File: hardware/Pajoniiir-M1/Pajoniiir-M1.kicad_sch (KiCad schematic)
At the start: 0 parts

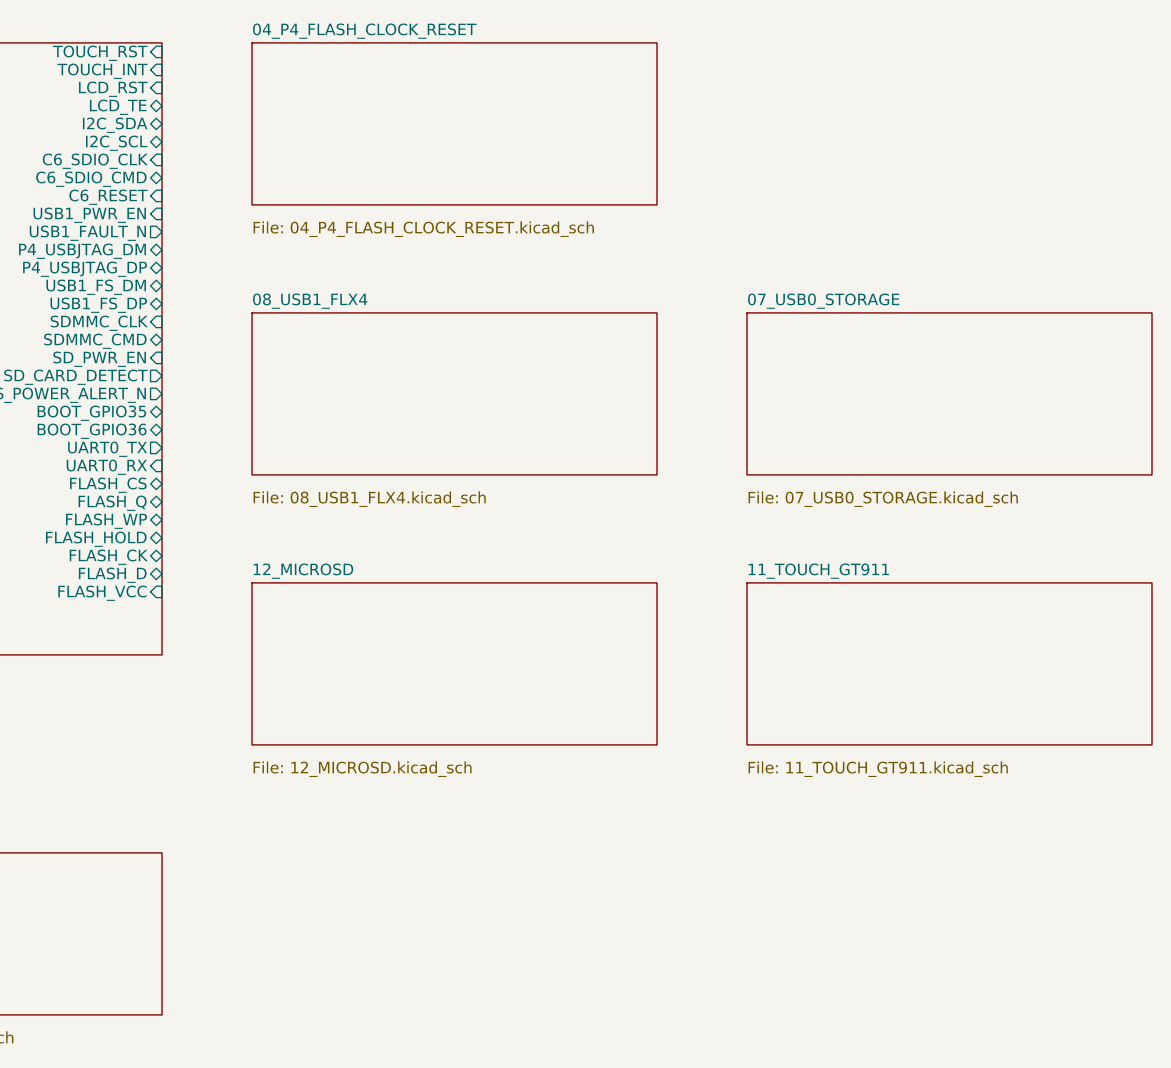
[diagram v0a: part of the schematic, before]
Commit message: hardware: capture P4 flash clock reset boot schematic
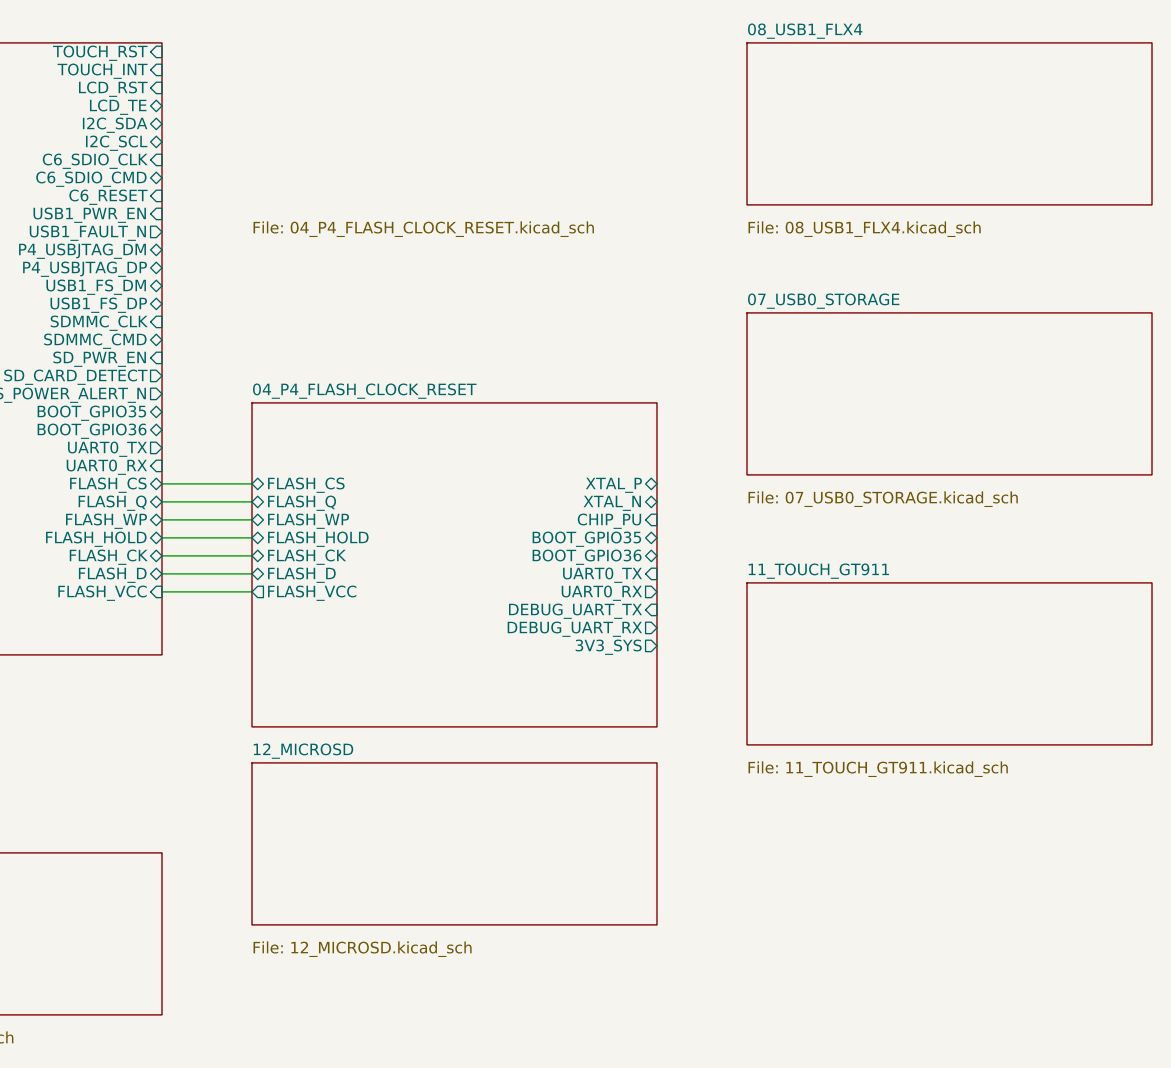
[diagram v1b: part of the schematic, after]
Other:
- sheet 04_P4_FLASH_CLOCK_RESET ports: added 3V3_SYS, BOOT_GPIO35, BOOT_GPIO36, CHIP_PU, DEBUG_UART_RX, DEBUG_UART_TX, FLASH_CK, FLASH_CS, FLASH_D, FLASH_HOLD, FLASH_Q, FLASH_VCC, FLASH_WP, UART0_RX, UART0_TX, XTAL_N, XTAL_P; removed none
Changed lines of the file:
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@@
   )
   (sheet
-    (at 185 20)
-    (size 45 18)
+    (at 185 60)
+    (size 45 36)
     (fields_autoplaced yes)
     (stroke (width 0.1524) (type solid))
     (fill (color 0 0 0 0.0000))
     (property "Sheetname" "04_P4_FLASH_CLOCK_RESET"
-      (at 185 19.2888 0)
+      (at 185 59.2888 0)
       (effects (font (size 1.27 1.27)) (justify left bottom))
     )
@@
       (effects (font (size 1.27 1.27)) (justify left top))
     )
+    (pin "FLASH_CS" bidirectional (at 185 69 180) (effects (font (size 1.27 1.27)) (justify left)))
+    (pin "FLASH_Q" bidirectional (at 185 71 180) (effects (font (size 1.27 1.27)) (justify left)))
+    (pin "FLASH_WP" bidirectional (at 185 73 180) (effects (font (size 1.27 1.27)) (justify left)))
+    (pin "FLASH_HOLD" bidirectional (at 185 75 180) (effects (font (size 1.27 1.27)) (justify left)))
+    (pin "FLASH_CK" bidirectional (at 185 77 180) (effects (font (size 1.27 1.27)) (justify left)))
+    (pin "FLASH_D" bidirectional (at 185 79 180) (effects (font (size 1.27 1.27)) (justify left)))
+    (pin "FLASH_VCC" output (at 185 81 180) (effects (font (size 1.27 1.27)) (justify left)))
+    (pin "XTAL_P" bidirectional (at 230 69 0) (effects (font (size 1.27 1.27)) (justify right)))
+    (pin "XTAL_N" bidirectional (at 230 71 0) (effects (font (size 1.27 1.27)) (justify right)))
+    (pin "CHIP_PU" input (at 230 73 0) (effects (font (size 1.27 1.27)) (justify right)))
+    (pin "BOOT_GPIO35" bidirectional (at 230 75 0) (effects (font (size 1.27 1.27)) (justify right)))
+    (pin "BOOT_GPIO36" bidirectional (at 230 77 0) (effects (font (size 1.27 1.27)) (justify right)))
+    (pin "UART0_TX" input (at 230 79 0) (effects (font (size 1.27 1.27)) (justify right)))
+    (pin "UART0_RX" output (at 230 81 0) (effects (font (size 1.27 1.27)) (justify right)))
+    (pin "DEBUG_UART_TX" input (at 230 83 0) (effects (font (size 1.27 1.27)) (justify right)))
+    (pin "DEBUG_UART_RX" output (at 230 85 0) (effects (font (size 1.27 1.27)) (justify right)))
+    (pin "3V3_SYS" output (at 230 87 0) (effects (font (size 1.27 1.27)) (justify right)))
     (instances
       (project "Pajoniiir-M1"
@@
   )
   (sheet
-    (at 185 50)
+    (at 240 20)
     (size 45 18)
     (fields_autoplaced yes)
@@
     (fill (color 0 0 0 0.0000))
     (property "Sheetname" "08_USB1_FLX4"
-      (at 185 49.2888 0)
+      (at 240 19.2888 0)
       (effects (font (size 1.27 1.27)) (justify left bottom))
     )
     (property "Sheetfile" "08_USB1_FLX4.kicad_sch"
-      (at 185 69.8246 0)
+      (at 240 39.8246 0)
       (effects (font (size 1.27 1.27)) (justify left top))
     )
@@
   )
   (sheet
-    (at 185 80)
+    (at 185 100)
     (size 45 18)
     (fields_autoplaced yes)
@@
     (fill (color 0 0 0 0.0000))
     (property "Sheetname" "12_MICROSD"
-      (at 185 79.2888 0)
+      (at 185 99.2888 0)
       (effects (font (size 1.27 1.27)) (justify left bottom))
     )
     (property "Sheetfile" "12_MICROSD.kicad_sch"
-      (at 185 99.8246 0)
+      (at 185 119.8246 0)
       (effects (font (size 1.27 1.27)) (justify left top))
     )
@@
   (wire (pts (xy 65 25) (xy 75 25)) (stroke (width 0) (type default)))
   (wire (pts (xy 120 23) (xy 125 23) (xy 125 25) (xy 130 25)) (stroke (width 0) (type default)))
+  (wire (pts (xy 175 69) (xy 185 69)) (stroke (width 0) (type default)))
+  (wire (pts (xy 175 71) (xy 185 71)) (stroke (width 0) (type default)))
+  (wire (pts (xy 175 73) (xy 185 73)) (stroke (width 0) (type default)))
+  (wire (pts (xy 175 75) (xy 185 75)) (stroke (width 0) (type default)))
+  (wire (pts (xy 175 77) (xy 185 77)) (stroke (width 0) (type default)))
+  (wire (pts (xy 175 79) (xy 185 79)) (stroke (width 0) (type default)))
+  (wire (pts (xy 175 81) (xy 185 81)) (stroke (width 0) (type default)))
   (sheet_instances (path "/" (page "1")))
   (embedded_fonts no)

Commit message: hardware: capture C6 WiFi ESP-Hosted SDIO schematic
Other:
- sheet 05_C6_WIFI ports: added 3V3_C6, C6_BOOT_GPIO8, C6_BOOT_GPIO9, C6_EN, C6_RESET, C6_SDIO_CLK, C6_SDIO_CMD, C6_SDIO_D0, C6_SDIO_D1, C6_SDIO_D2, C6_SDIO_D3, C6_UART_RX, C6_UART_TX; removed none
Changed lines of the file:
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@@
   (sheet
     (at 20 50)
-    (size 45 18)
+    (size 45 42)
     (fields_autoplaced yes)
     (stroke (width 0.1524) (type solid))
@@
     )
     (property "Sheetfile" "05_C6_WIFI.kicad_sch"
-      (at 20 69.8246 0)
-      (effects (font (size 1.27 1.27)) (justify left top))
-    )
+      (at 20 93.8246 0)
+      (effects (font (size 1.27 1.27)) (justify left top))
+    )
+    (pin "3V3_C6" output (at 20 57 180) (effects (font (size 1.27 1.27)) (justify left)))
+    (pin "C6_RESET" output (at 20 61 180) (effects (font (size 1.27 1.27)) (justify left)))
+    (pin "C6_SDIO_D0" bidirectional (at 65 55 0) (effects (font (size 1.27 1.27)) (justify right)))
+    (pin "C6_SDIO_D1" bidirectional (at 65 57 0) (effects (font (size 1.27 1.27)) (justify right)))
+    (pin "C6_SDIO_D2" bidirectional (at 65 59 0) (effects (font (size 1.27 1.27)) (justify right)))
+    (pin "C6_SDIO_D3" bidirectional (at 65 61 0) (effects (font (size 1.27 1.27)) (justify right)))
+    (pin "C6_SDIO_CLK" bidirectional (at 65 63 0) (effects (font (size 1.27 1.27)) (justify right)))
+    (pin "C6_SDIO_CMD" bidirectional (at 65 65 0) (effects (font (size 1.27 1.27)) (justify right)))
+    (pin "C6_UART_TX" input (at 65 69 0) (effects (font (size 1.27 1.27)) (justify right)))
+    (pin "C6_UART_RX" output (at 65 71 0) (effects (font (size 1.27 1.27)) (justify right)))
+    (pin "C6_BOOT_GPIO8" bidirectional (at 65 75 0) (effects (font (size 1.27 1.27)) (justify right)))
+    (pin "C6_BOOT_GPIO9" bidirectional (at 65 77 0) (effects (font (size 1.27 1.27)) (justify right)))
+    (pin "C6_EN" input (at 65 79 0) (effects (font (size 1.27 1.27)) (justify right)))
     (instances
       (project "Pajoniiir-M1"
@@
   )
   (sheet
-    (at 20 80)
+    (at 20 105)
     (size 45 18)
     (fields_autoplaced yes)
@@
     (fill (color 0 0 0 0.0000))
     (property "Sheetname" "09_AUDIO_PCM5102A"
-      (at 20 79.2888 0)
+      (at 20 104.2888 0)
       (effects (font (size 1.27 1.27)) (justify left bottom))
     )
     (property "Sheetfile" "09_AUDIO_PCM5102A.kicad_sch"
-      (at 20 99.8246 0)
+      (at 20 124.8246 0)
       (effects (font (size 1.27 1.27)) (justify left top))
     )
@@
   (wire (pts (xy 175 79) (xy 185 79)) (stroke (width 0) (type default)))
   (wire (pts (xy 175 81) (xy 185 81)) (stroke (width 0) (type default)))
+  (label "3V3_C6" (at 20 57 180) (effects (font (size 1.27 1.27))))
+  (label "C6_RESET" (at 20 61 180) (effects (font (size 1.27 1.27))))
+  (label "C6_SDIO_D0" (at 65 55 0) (effects (font (size 1.27 1.27))))
+  (label "C6_SDIO_D1" (at 65 57 0) (effects (font (size 1.27 1.27))))
+  (label "C6_SDIO_D2" (at 65 59 0) (effects (font (size 1.27 1.27))))
+  (label "C6_SDIO_D3" (at 65 61 0) (effects (font (size 1.27 1.27))))
+  (label "C6_SDIO_CLK" (at 65 63 0) (effects (font (size 1.27 1.27))))
+  (label "C6_SDIO_CMD" (at 65 65 0) (effects (font (size 1.27 1.27))))
+  (label "C6_UART_TX" (at 65 69 0) (effects (font (size 1.27 1.27))))
+  (label "C6_UART_RX" (at 65 71 0) (effects (font (size 1.27 1.27))))
+  (label "C6_BOOT_GPIO8" (at 65 75 0) (effects (font (size 1.27 1.27))))
+  (label "C6_BOOT_GPIO9" (at 65 77 0) (effects (font (size 1.27 1.27))))
+  (label "C6_EN" (at 65 79 0) (effects (font (size 1.27 1.27))))
+  (label "C6_SDIO_D0" (at 130 31 180) (effects (font (size 1.27 1.27))))
+  (label "C6_SDIO_D1" (at 130 33 180) (effects (font (size 1.27 1.27))))
+  (label "C6_SDIO_D2" (at 130 35 180) (effects (font (size 1.27 1.27))))
+  (label "C6_SDIO_D3" (at 130 37 180) (effects (font (size 1.27 1.27))))
+  (label "C6_SDIO_CLK" (at 175 33 0) (effects (font (size 1.27 1.27))))
+  (label "C6_SDIO_CMD" (at 175 35 0) (effects (font (size 1.27 1.27))))
+  (label "C6_RESET" (at 175 37 0) (effects (font (size 1.27 1.27))))
+  (label "3V3_C6" (at 120 31 0) (effects (font (size 1.27 1.27))))
   (sheet_instances (path "/" (page "1")))
   (embedded_fonts no)

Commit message: hardware: wire dual USB power hierarchy
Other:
- sheet 06_USB_POWER ports: added 3V3_SYS, 5V_SYS, USB0_FAULT_N, USB0_PWR_EN, USB0_VBUS, USB1_FAULT_N, USB1_PWR_EN, USB1_VBUS; removed none
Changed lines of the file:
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@@
   (sheet
     (at 75 50)
-    (size 45 18)
+    (size 45 38)
     (fields_autoplaced yes)
     (stroke (width 0.1524) (type solid))
@@
     )
     (property "Sheetfile" "06_USB_POWER.kicad_sch"
-      (at 75 69.8246 0)
-      (effects (font (size 1.27 1.27)) (justify left top))
-    )
+      (at 75 89.8246 0)
+      (effects (font (size 1.27 1.27)) (justify left top))
+    )
+    (pin "5V_SYS" output (at 75 55 180) (effects (font (size 1.27 1.27)) (justify left)))
+    (pin "3V3_SYS" output (at 75 59 180) (effects (font (size 1.27 1.27)) (justify left)))
+    (pin "USB0_PWR_EN" output (at 120 55 0) (effects (font (size 1.27 1.27)) (justify right)))
+    (pin "USB0_FAULT_N" input (at 120 59 0) (effects (font (size 1.27 1.27)) (justify right)))
+    (pin "USB1_PWR_EN" output (at 120 63 0) (effects (font (size 1.27 1.27)) (justify right)))
+    (pin "USB1_FAULT_N" input (at 120 67 0) (effects (font (size 1.27 1.27)) (justify right)))
+    (pin "USB0_VBUS" input (at 120 73 0) (effects (font (size 1.27 1.27)) (justify right)))
+    (pin "USB1_VBUS" input (at 120 77 0) (effects (font (size 1.27 1.27)) (justify right)))
     (instances
       (project "Pajoniiir-M1"
@@
   )
   (sheet
-    (at 75 80)
+    (at 75 105)
     (size 45 18)
     (fields_autoplaced yes)
@@
     (fill (color 0 0 0 0.0000))
     (property "Sheetname" "10_DISPLAY_MIPI"
-      (at 75 79.2888 0)
+      (at 75 104.2888 0)
       (effects (font (size 1.27 1.27)) (justify left bottom))
     )
     (property "Sheetfile" "10_DISPLAY_MIPI.kicad_sch"
-      (at 75 99.8246 0)
+      (at 75 124.8246 0)
       (effects (font (size 1.27 1.27)) (justify left top))
     )
@@
   (label "C6_RESET" (at 175 37 0) (effects (font (size 1.27 1.27))))
   (label "3V3_C6" (at 120 31 0) (effects (font (size 1.27 1.27))))
+  (label "5V_SYS" (at 75 55 180) (effects (font (size 1.27 1.27))))
+  (label "3V3_SYS" (at 75 59 180) (effects (font (size 1.27 1.27))))
+  (label "USB0_PWR_EN" (at 120 55 0) (effects (font (size 1.27 1.27))))
+  (label "USB0_FAULT_N" (at 120 59 0) (effects (font (size 1.27 1.27))))
+  (label "USB1_PWR_EN" (at 120 63 0) (effects (font (size 1.27 1.27))))
+  (label "USB1_FAULT_N" (at 120 67 0) (effects (font (size 1.27 1.27))))
+  (label "USB0_VBUS" (at 120 73 0) (effects (font (size 1.27 1.27))))
+  (label "USB1_VBUS" (at 120 77 0) (effects (font (size 1.27 1.27))))
+  (label "5V_SYS" (at 65 25 0) (effects (font (size 1.27 1.27))))
+  (label "3V3_SYS" (at 120 23 0) (effects (font (size 1.27 1.27))))
+  (label "USB0_PWR_EN" (at 130 39 180) (effects (font (size 1.27 1.27))))
+  (label "USB0_FAULT_N" (at 130 41 180) (effects (font (size 1.27 1.27))))
+  (label "USB1_PWR_EN" (at 175 39 0) (effects (font (size 1.27 1.27))))
+  (label "USB1_FAULT_N" (at 175 41 0) (effects (font (size 1.27 1.27))))
   (sheet_instances (path "/" (page "1")))
   (embedded_fonts no)

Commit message: hardware: wire USB0 storage hierarchy
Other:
- sheet 07_USB0_STORAGE ports: added USB0_HS_DM, USB0_HS_DP, USB0_VBUS; removed none
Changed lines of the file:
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@@
       (effects (font (size 1.27 1.27)) (justify left top))
     )
+    (pin "USB0_HS_DM" bidirectional (at 240 55 180) (effects (font (size 1.27 1.27)) (justify left)))
+    (pin "USB0_HS_DP" bidirectional (at 240 59 180) (effects (font (size 1.27 1.27)) (justify left)))
+    (pin "USB0_VBUS" output (at 240 63 180) (effects (font (size 1.27 1.27)) (justify left)))
     (instances
       (project "Pajoniiir-M1"
@@
   (label "USB1_PWR_EN" (at 175 39 0) (effects (font (size 1.27 1.27))))
   (label "USB1_FAULT_N" (at 175 41 0) (effects (font (size 1.27 1.27))))
+  (label "USB0_HS_DM" (at 240 55 180) (effects (font (size 1.27 1.27))))
+  (label "USB0_HS_DP" (at 240 59 180) (effects (font (size 1.27 1.27))))
+  (label "USB0_VBUS" (at 240 63 180) (effects (font (size 1.27 1.27))))
+  (label "USB0_HS_DM" (at 130 45 180) (effects (font (size 1.27 1.27))))
+  (label "USB0_HS_DP" (at 130 47 180) (effects (font (size 1.27 1.27))))
+  (label "USB0_VBUS" (at 120 73 0) (effects (font (size 1.27 1.27))))
   (sheet_instances (path "/" (page "1")))
   (embedded_fonts no)
